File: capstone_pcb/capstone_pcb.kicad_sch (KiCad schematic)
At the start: 46 parts, among them IC6 BSS138, P1 MHDR1X5, Q1 BSS138, U2 BMI270, U3 NRF52840-QIAA-R, U4 MAX30102EFD+T, X1 32MHz, X2 32.768kHz

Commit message: Add files via upload
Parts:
- added U1: AMS1117-3.3, Package_TO_SOT_SMD:SOT-223-3_TabPin2, symbol Regulator_Linear:AMS1117-3.3
- added U5: AMS1117-1.8, Package_TO_SOT_SMD:SOT-223-3_TabPin2, symbol Regulator_Linear:AMS1117-1.8
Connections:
- net +1V8: now also U5.2 (VO)
- net +3.3V: now also U1.2 (VO)
- net Earth: now also U1.1 (GND), U5.1 (GND)
- net VBAT: now also U1.3 (VI), U5.3 (VI)
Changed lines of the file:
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@@
+    )
+  )
+  (global_label "VBAT" (shape input) (at 302.26 199.39 180) (fields_autoplaced)
+    (effects (font (size 1.27 1.27)) (justify right))
+    (property "Intersheetrefs" "${INTERSHEET_REFS}" (at 294.86 199.39 0)
+      (effects (font (size 1.27 1.27)) (justify right) hide)
     )
   )
@@
     (effects (font (size 1.27 1.27)) (justify right))
     (property "Intersheetrefs" "${INTERSHEET_REFS}" (at 160.8448 165.1 0)
+      (effects (font (size 1.27 1.27)) (justify right) hide)
+    )
+  )
+  (global_label "VBAT" (shape input) (at 302.26 219.71 180) (fields_autoplaced)
+    (effects (font (size 1.27 1.27)) (justify right))
+    (property "Intersheetrefs" "${INTERSHEET_REFS}" (at 294.86 219.71 0)
       (effects (font (size 1.27 1.27)) (justify right) hide)
     )
@@
     )
   )
+  (symbol (lib_id "Regulator_Linear:AMS1117-1.8") (at 309.88 219.71 0) (unit 1)
+    (in_bom yes) (on_board yes) (dnp no) (fields_autoplaced)
+    (property "Reference" "U5" (at 309.88 213.36 0)
+      (effects (font (size 1.27 1.27)))
+    )
+    (property "Value" "AMS1117-1.8" (at 309.88 215.9 0)
+      (effects (font (size 1.27 1.27)))
+    )
+    (property "Footprint" "Package_TO_SOT_SMD:SOT-223-3_TabPin2" (at 309.88 214.63 0)
+      (effects (font (size 1.27 1.27)) hide)
+    )
+    (property "Datasheet" "http://www.advanced-monolithic.com/pdf/ds1117.pdf" (at 312.42 226.06 0)
+      (effects (font (size 1.27 1.27)) hide)
+    )
+    (pin "1")
+    (pin "2")
+    (pin "3")
+    (instances
+      (project "capstone_pcb"
+        (path "/277c13c0-adeb-4e61-8bb9-47465b7f1900"
+          (reference "U5") (unit 1)
+        )
+      )
+    )
+  )
   (symbol (lib_id "power:GNDREF") (at 21.59 198.12 270) (unit 1)
     (in_bom yes) (on_board yes) (dnp no) (fields_autoplaced)
@@
         (path "/277c13c0-adeb-4e61-8bb9-47465b7f1900"
           (reference "#PWR04") (unit 1)
+        )
+      )
+    )
+  )
+  (symbol (lib_id "Regulator_Linear:AMS1117-3.3") (at 309.88 199.39 0) (unit 1)
+    (in_bom yes) (on_board yes) (dnp no) (fields_autoplaced)
+    (property "Reference" "U1" (at 309.88 193.04 0)
+      (effects (font (size 1.27 1.27)))
+    )
+    (property "Value" "AMS1117-3.3" (at 309.88 195.58 0)
+      (effects (font (size 1.27 1.27)))
+    )
+    (property "Footprint" "Package_TO_SOT_SMD:SOT-223-3_TabPin2" (at 309.88 194.31 0)
+      (effects (font (size 1.27 1.27)) hide)
+    )
+    (property "Datasheet" "http://www.advanced-monolithic.com/pdf/ds1117.pdf" (at 312.42 205.74 0)
+      (effects (font (size 1.27 1.27)) hide)
+    )
+    (pin "1")
+    (pin "2")
+    (pin "3")
+    (instances
+      (project "capstone_pcb"
+        (path "/277c13c0-adeb-4e61-8bb9-47465b7f1900"
+          (reference "U1") (unit 1)
         )
       )
@@
     )
   )
+  (symbol (lib_id "power:GNDREF") (at 309.88 227.33 0) (unit 1)
+    (in_bom yes) (on_board yes) (dnp no) (fields_autoplaced)
+    (property "Reference" "#PWR032" (at 309.88 233.68 0)
+      (effects (font (size 1.27 1.27)) hide)
+    )
+    (property "Value" "GNDREF" (at 309.88 232.41 0)
+      (effects (font (size 1.27 1.27)) hide)
+    )
+    (property "Footprint" "" (at 309.88 227.33 0)
+      (effects (font (size 1.27 1.27)) hide)
+    )
+    (property "Datasheet" "" (at 309.88 227.33 0)
+      (effects (font (size 1.27 1.27)) hide)
+    )
+    (pin "1")
+    (instances
+      (project "capstone_pcb"
+        (path "/277c13c0-adeb-4e61-8bb9-47465b7f1900"
+          (reference "#PWR032") (unit 1)
+        )
+      )
+    )
+  )
   (symbol (lib_id "Device:C") (at 165.1 143.51 180) (unit 1)
     (in_bom no) (on_board yes) (dnp yes) (fields_autoplaced)
@@
         (path "/277c13c0-adeb-4e61-8bb9-47465b7f1900"
           (reference "C13") (unit 1)
+        )
+      )
+    )
+  )
+  (symbol (lib_id "power:+3.3V") (at 317.5 199.39 270) (unit 1)
+    (in_bom yes) (on_board yes) (dnp no) (fields_autoplaced)
+    (property "Reference" "#PWR029" (at 313.69 199.39 0)
+      (effects (font (size 1.27 1.27)) hide)
+    )
+    (property "Value" "+3.3V" (at 321.31 199.39 90)
+      (effects (font (size 1.27 1.27)) (justify left))
+    )
+    (property "Footprint" "" (at 317.5 199.39 0)
+      (effects (font (size 1.27 1.27)) hide)
+    )
+    (property "Datasheet" "" (at 317.5 199.39 0)
+      (effects (font (size 1.27 1.27)) hide)
+    )
+    (pin "1")
+    (instances
+      (project "capstone_pcb"
+        (path "/277c13c0-adeb-4e61-8bb9-47465b7f1900"
+          (reference "#PWR029") (unit 1)
         )
       )
@@
     )
   )
+  (symbol (lib_id "power:+1V8") (at 317.5 219.71 270) (unit 1)
+    (in_bom yes) (on_board yes) (dnp no) (fields_autoplaced)
+    (property "Reference" "#PWR033" (at 313.69 219.71 0)
+      (effects (font (size 1.27 1.27)) hide)
+    )
+    (property "Value" "+1V8" (at 321.31 219.71 90)
+      (effects (font (size 1.27 1.27)) (justify left))
+    )
+    (property "Footprint" "" (at 317.5 219.71 0)
+      (effects (font (size 1.27 1.27)) hide)
+    )
+    (property "Datasheet" "" (at 317.5 219.71 0)
+      (effects (font (size 1.27 1.27)) hide)
+    )
+    (pin "1")
+    (instances
+      (project "capstone_pcb"
+        (path "/277c13c0-adeb-4e61-8bb9-47465b7f1900"
+          (reference "#PWR033") (unit 1)
+        )
+      )
+    )
+  )
   (symbol (lib_id "Device:R_US") (at 143.51 210.82 0) (unit 1)
     (in_bom yes) (on_board yes) (dnp no) (fields_autoplaced)
@@
         )
       )
+    )
+  )
+  (symbol (lib_id "power:GNDREF") (at 309.88 207.01 0) (unit 1)
+    (in_bom yes) (on_board yes) (dnp no) (fields_autoplaced)
+    (property "Reference" "#PWR031" (at 309.88 213.36 0)
+      (effects (font (size 1.27 1.27)) hide)
+    )
+    (property "Value" "GNDREF" (at 309.88 212.09 0)
+      (effects (font (size 1.27 1.27)) hide)
+    )
+    (property "Footprint" "" (at 309.88 207.01 0)
+      (effects (font (size 1.27 1.27)) hide)
+    )
+    (property "Datasheet" "" (at 309.88 207.01 0)
+      (effects (font (size 1.27 1.27)) hide)
+    )
+    (pin "1")
+    (instances
+      (project "capstone_pcb"
+        (path "/277c13c0-adeb-4e61-8bb9-47465b7f1900"
+          (reference "#PWR031") (unit 1)
+        )
+      )

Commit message: pcb schematic
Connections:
- net VBUS_nrF is gone; now on net VBUS: U3.AD2 (VBUS)
- no-connect marks 51 -> 61
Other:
- moved on the sheet: C14, C17, C18, C5, X2

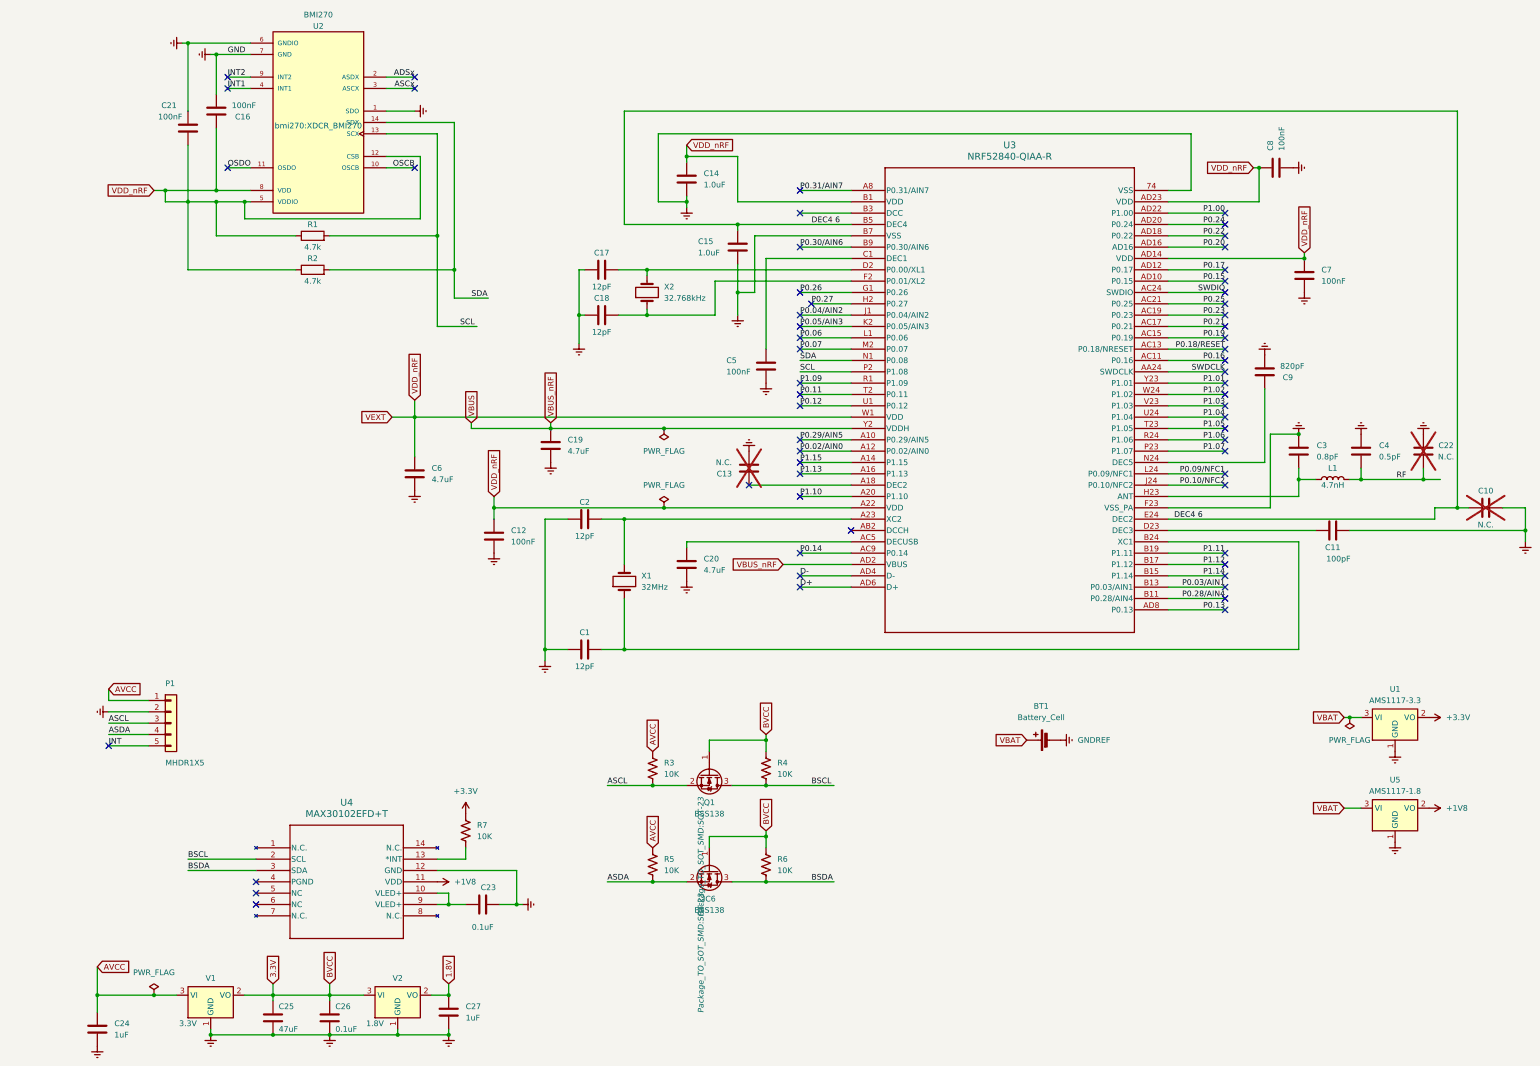
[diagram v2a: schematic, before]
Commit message: PCB layout complete
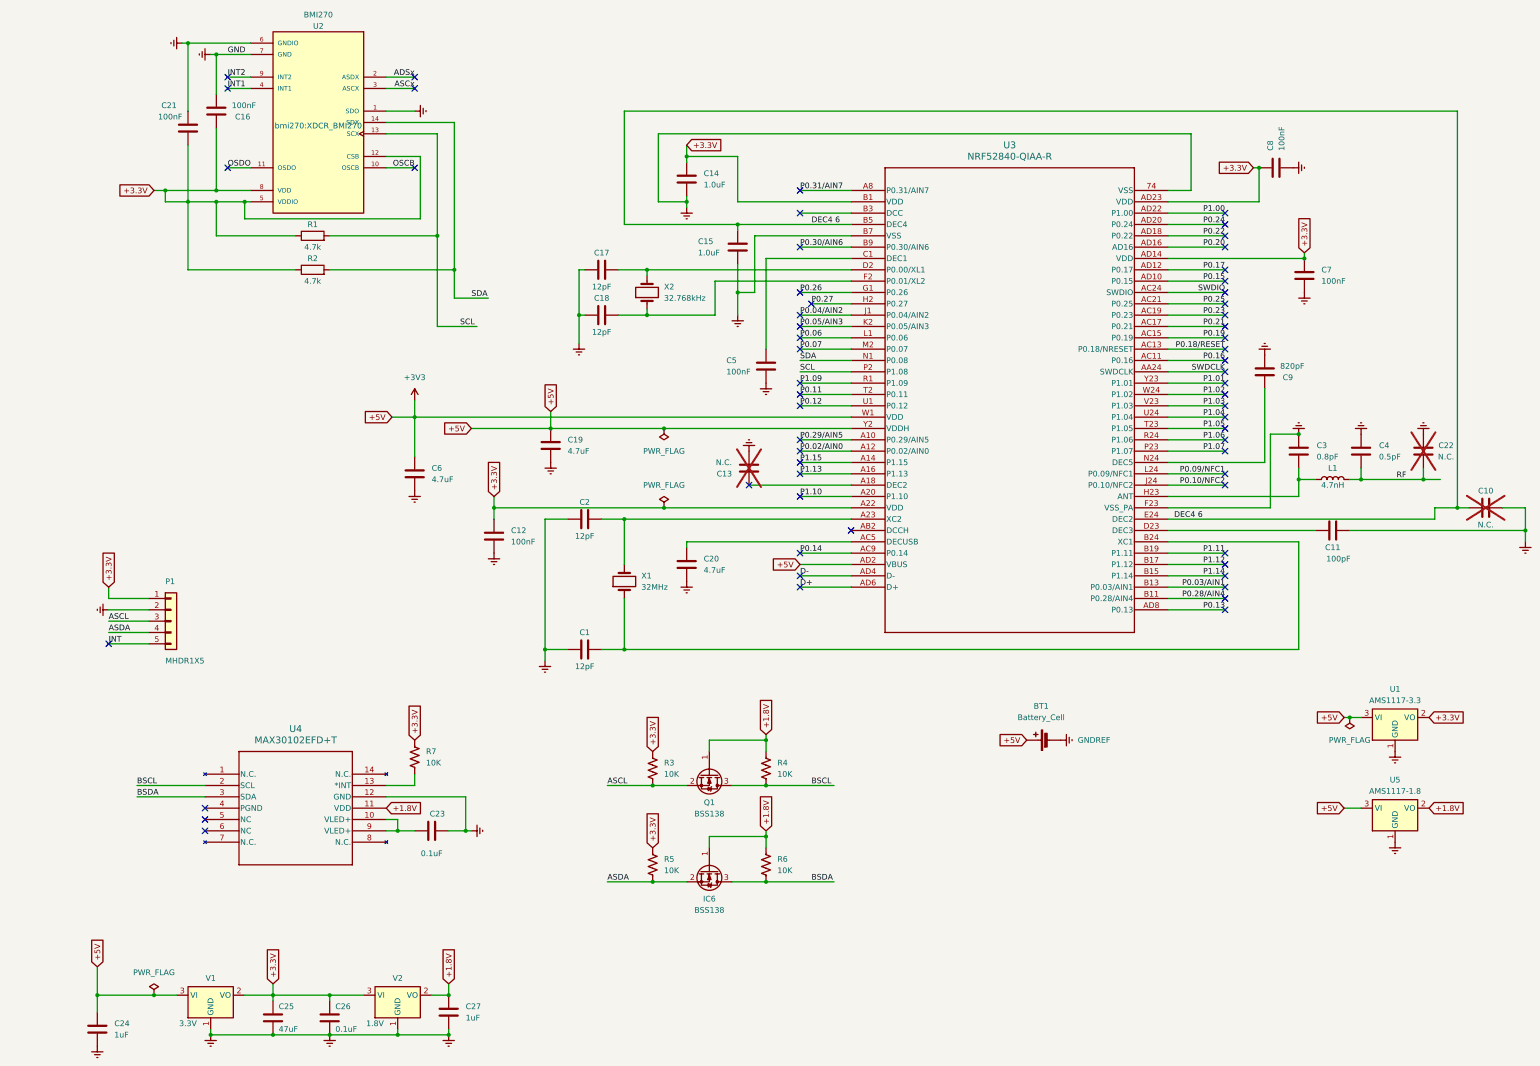
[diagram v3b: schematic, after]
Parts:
- U3: footprint Library:nrf52840_qiaa_r -> nrf:nrf52840_qiaa_r
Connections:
- net 1.8V is gone; now on net +1.8V: C27.1, V2.2 (VO)
- net VBUS is gone; now on net +3V3: C19.1, U3.AD2 (VBUS), U3.Y2 (VDDH)
- net +3.3V: now also C12.1, C14.1, C16.1, C21.1, C25.1, C26.1, C7.1, C8.1, P1.1 (Pin_1), R1.1, R2.1, R3.1, R5.1, U2.12 (CSB), U2.5 (VDDIO), U2.8 (VDD), U3.A22 (VDD), U3.AD14 (VDD), U3.AD23 (VDD), U3.B1 (VDD), V1.2 (VO), V2.3 (VI)
- net +1V8 renamed +1.8V
- net +1.8V: now also IC6.1 (G), Q1.1 (G), R4.1, R6.1
- removed net 3.3V: C25.1, C26.1, IC6.1 (G), Q1.1 (G), R4.1, R6.1, V1.2 (VO), V2.3 (VI)
- removed net AVCC: C24.1, P1.1 (Pin_1), R3.1, R5.1, V1.3 (VI)
- net VBAT renamed +3V3
- net +3V3: now also C24.1, C6.1, U3.W1 (VDD), V1.3 (VI)
- removed net VDD_nRF: C12.1, C14.1, C16.1, C21.1, C6.1, C7.1, C8.1, R1.1, R2.1, U2.12 (CSB), U2.5 (VDDIO), U2.8 (VDD), U3.A22 (VDD), U3.AD14 (VDD), U3.AD23 (VDD), U3.B1 (VDD), U3.W1 (VDD)
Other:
- moved on the sheet: C23, P1, R7, U4
